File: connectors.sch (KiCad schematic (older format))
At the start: 2 parts, among them P1 CONN_02X06, P3 CONN_02X04

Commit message: Remove VCC from UART-DBG connector
 * VCC of a USB-TTL connector may not be connected to VCC of the board.
     The usb will put 3.3V (or 5V) on this pin, so we will create a short
     circuit if we connect the TLL and use a battery as supply.

Signed-off-by: Philip Luyckx <philip.luyckx@gmail.com>
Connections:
- net VCC: no longer P1.6 (P6)
- no-connect marks 3 -> 4
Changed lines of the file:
@@
 $EndComp
 NoConn ~ 3200 3950
-$Comp
-L VCC #PWR017
-U 1 1 5669F115
-P 3500 3950
-F 0 "#PWR017" H 3500 3800 50  0001 C CNN
-F 1 "VCC" H 3500 4100 50  0000 C CNN
-F 2 "" H 3500 3950 60  0000 C CNN
-F 3 "" H 3500 3950 60  0000 C CNN
-	1    3500 3950
-	1    0    0    -1
-$EndComp
 NoConn ~ 3200 4350
 Wire Wire Line
@@
 Wire Wire Line
 	2200 4050 2200 4450
-Wire Wire Line
-	3200 4050 3500 4050
-Wire Wire Line
-	3500 4050 3500 3950
+NoConn ~ 3200 4050
 $EndSCHEMATC

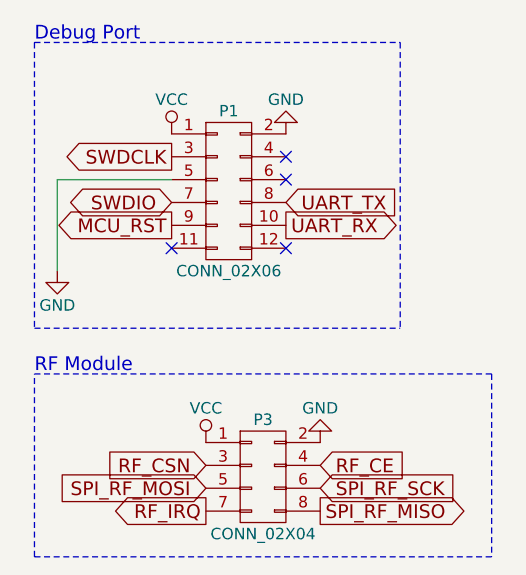
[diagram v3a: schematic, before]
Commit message: Finish work on V2
 * Rework layout
 * Reassign mcu pins
 * Add a capacitor for the RF module

Signed-off-by: Philip Luyckx <philip.luyckx@gmail.com>
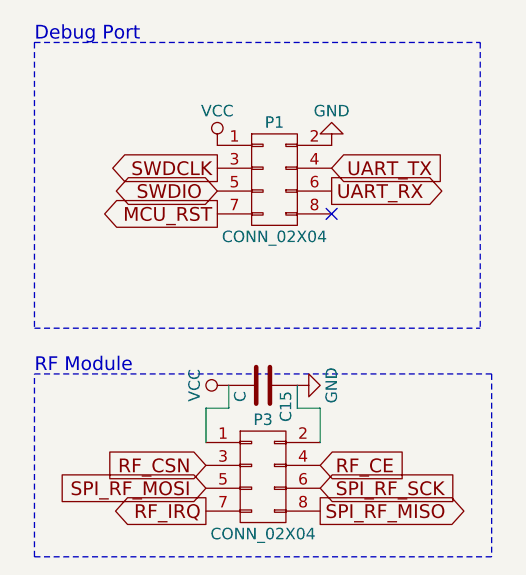
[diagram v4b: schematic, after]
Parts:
- removed P1: CONN_02X06, Pin_Headers:Pin_Header_Straight_2x06, symbol CONN_02X06
- added C15: C, Resistors_SMD:R_0805, symbol C
- added P1: CONN_02X04, Socket_Strips:Socket_Strip_Straight_2x04, symbol CONN_02X04
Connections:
- net GND: now also C15.1, P1.2 (P2)
- net MCU_RST: now also P1.7 (P7)
- net SWDCLK: now also P1.3 (P3)
- net SWDIO: now also P1.5 (P5)
- net UART_RX: now also P1.6 (P6)
- net UART_TX: now also P1.4 (P4)
- net VCC: now also C15.2, P1.1 (P1)
- no-connect marks 4 -> 1
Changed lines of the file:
@@
 L VCC #PWR012
 U 1 1 565F5F2C
-P 2700 3850
-F 0 "#PWR012" H 2700 3700 50  0001 C CNN
-F 1 "VCC" H 2700 4000 50  0000 C CNN
-F 2 "" H 2700 3850 60  0000 C CNN
-F 3 "" H 2700 3850 60  0000 C CNN
-	1    2700 3850
+P 2900 3900
+F 0 "#PWR012" H 2900 3750 50  0001 C CNN
+F 1 "VCC" H 2900 4050 50  0000 C CNN
+F 2 "" H 2900 3900 60  0000 C CNN
+F 3 "" H 2900 3900 60  0000 C CNN
+	1    2900 3900
 	1    0    0    -1
 $EndComp
-$Comp
-L GND #PWR013
-U 1 1 565F5F42
-P 2200 4450
-F 0 "#PWR013" H 2200 4200 50  0001 C CNN
-F 1 "GND" H 2200 4300 50  0000 C CNN
-F 2 "" H 2200 4450 60  0000 C CNN
-F 3 "" H 2200 4450 60  0000 C CNN
-	1    2200 4450
-	1    0    0    -1
-$EndComp
-Text GLabel 2700 4250 0    60   Output ~ 0
+Text GLabel 2900 4200 0    60   Output ~ 0
 MCU_RST
-Text GLabel 2700 4150 0    60   BiDi ~ 0
+Text GLabel 2900 4100 0    60   BiDi ~ 0
 SWDIO
-Text GLabel 2700 3950 0    60   Output ~ 0
+Text GLabel 2900 4000 0    60   Output ~ 0
 SWDCLK
-Text GLabel 3200 4250 2    60   Output ~ 0
+Text GLabel 3400 4100 2    60   Output ~ 0
 UART_RX
-Text GLabel 3200 4150 2    60   Input ~ 0
+Text GLabel 3400 4000 2    60   Input ~ 0
 UART_TX
 $Comp
@@
 $EndComp
 $Comp
-L VCC #PWR014
+L VCC #PWR013
 U 1 1 56622A6F
-P 2850 5200
-F 0 "#PWR014" H 2850 5050 50  0001 C CNN
-F 1 "VCC" H 2850 5350 50  0000 C CNN
-F 2 "" H 2850 5200 60  0000 C CNN
-F 3 "" H 2850 5200 60  0000 C CNN
-	1    2850 5200
-	1    0    0    -1
+P 2950 4950
+F 0 "#PWR013" H 2950 4800 50  0001 C CNN
+F 1 "VCC" H 2950 5100 50  0000 C CNN
+F 2 "" H 2950 4950 60  0000 C CNN
+F 3 "" H 2950 4950 60  0000 C CNN
+	1    2950 4950
+	0    -1   -1   0
 $EndComp
 $Comp
-L GND #PWR015
+L GND #PWR014
 U 1 1 56622A8F
-P 3350 5200
-F 0 "#PWR015" H 3350 4950 50  0001 C CNN
-F 1 "GND" H 3350 5050 50  0000 C CNN
-F 2 "" H 3350 5200 60  0000 C CNN
-F 3 "" H 3350 5200 60  0000 C CNN
-	1    3350 5200
-	-1   0    0    1
+P 3250 4950
+F 0 "#PWR014" H 3250 4700 50  0001 C CNN
+F 1 "GND" H 3250 4800 50  0000 C CNN
+F 2 "" H 3250 4950 60  0000 C CNN
+F 3 "" H 3250 4950 60  0000 C CNN
+	1    3250 4950
+	0    -1   -1   0
 $EndComp
 Text GLabel 2850 5300 0    60   Input ~ 0
@@
 Text Notes 2100 4900 0    60   ~ 0
 RF Module
-Wire Notes Line
-	3700 3450 3700 4700
-Wire Notes Line
-	2100 3450 2100 4700
-Wire Notes Line
-	2100 3450 3700 3450
 Text Notes 2100 3450 0    60   ~ 0
 Debug Port
 Wire Notes Line
-	2100 4700 3700 4700
+	2100 4700 4050 4700
 $Comp
-L CONN_02X06 P1
-U 1 1 5669EE90
-P 2950 4100
-F 0 "P1" H 2950 4450 50  0000 C CNN
-F 1 "CONN_02X06" H 2950 3750 50  0000 C CNN
-F 2 "Pin_Headers:Pin_Header_Straight_2x06" H 2950 2900 60  0001 C CNN
-F 3 "" H 2950 2900 60  0000 C CNN
-	1    2950 4100
+L GND #PWR015
+U 1 1 5669F0F1
+P 3400 3900
+F 0 "#PWR015" H 3400 3650 50  0001 C CNN
+F 1 "GND" H 3400 3750 50  0000 C CNN
+F 2 "" H 3400 3900 60  0000 C CNN
+F 3 "" H 3400 3900 60  0000 C CNN
+	1    3400 3900
+	-1   0    0    1
+$EndComp
+NoConn ~ 3400 4200
+Wire Notes Line
+	2100 3450 4050 3450
+Wire Notes Line
+	4050 3450 4050 4700
+Wire Notes Line
+	2100 3450 2100 4700
+$Comp
+L CONN_02X04 P1
+U 1 1 56DBFF1C
+P 3150 4050
+F 0 "P1" H 3150 4300 50  0000 C CNN
+F 1 "CONN_02X04" H 3150 3800 50  0000 C CNN
+F 2 "Socket_Strips:Socket_Strip_Straight_2x04" H 3150 2850 50  0001 C CNN
+F 3 "" H 3150 2850 50  0000 C CNN
+	1    3150 4050
 	1    0    0    -1
 $EndComp
-NoConn ~ 2700 4350
 $Comp
-L GND #PWR016
-U 1 1 5669F0F1
-P 3200 3850
-F 0 "#PWR016" H 3200 3600 50  0001 C CNN
-F 1 "GND" H 3200 3700 50  0000 C CNN
-F 2 "" H 3200 3850 60  0000 C CNN
-F 3 "" H 3200 3850 60  0000 C CNN
-	1    3200 3850
-	-1   0    0    1
+L C C15
+U 1 1 56DC195B
+P 3100 4950
+F 0 "C15" H 3125 5050 50  0000 L CNN
+F 1 "C" H 3125 4850 50  0000 L CNN
+F 2 "Resistors_SMD:R_0805" H 3138 4800 50  0001 C CNN
+F 3 "" H 3100 4950 50  0000 C CNN
+	1    3100 4950
+	0    1    1    0
 $EndComp
-NoConn ~ 3200 3950
-NoConn ~ 3200 4350
 Wire Wire Line
-	2700 4050 2200 4050
+	2850 5200 2850 5050
 Wire Wire Line
-	2200 4050 2200 4450
-NoConn ~ 3200 4050
+	2850 5050 2950 5050
+Wire Wire Line
+	2950 5050 2950 4950
+Wire Wire Line
+	3350 5200 3350 5050
+Wire Wire Line
+	3350 5050 3250 5050
+Wire Wire Line
+	3250 5050 3250 4950
 $EndSCHEMATC
